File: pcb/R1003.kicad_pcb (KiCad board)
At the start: 2 copper layers, 45 x 33.3 mm, 27 parts, among them J1 PCIEXPRESS-X1, J2 CONN_01X03, J3 CONN254P-02X04, U1 EFM8BB10F2G

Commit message: getting ready for release
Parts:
- removed C1: 0.1u, Capacitors_SMD:C_0603
- removed G***: LOGO, pluggee:pluggee-LOGO-131X127
- removed G***: LOGO, pluggee:pluggee-QRNEG-127X127
- removed R1, R2, R3, R4, R5, R6, R7, R8: 10k, Resistors_SMD:R_0603
- removed U1: EFM8BB10F2G, Main:QFN50P300X300X75-20NT170X170
- added A1: ART, pluggee:pluggeeLabsIcon-11x6, F.Cu at (131.4, 75.3)
- added J10: SOCKET254P-01X02, Main:SOCKET254P-01X02_2, B.Cu at (143.0, 76.0)
- added J11: SOCKET254P-01X02, Main:SOCKET254P-01X02_2, B.Cu at (155.0, 76.0)
- added J12: SOCKET254P-01X02, Main:SOCKET254P-01X02_2, B.Cu at (155.0, 86.0)
- added J13: SOCKET254P-01X02, Main:SOCKET254P-01X02_2, B.Cu at (164.0, 90.0)
- added J4: SOCKET254P-01X02, Main:SOCKET254P-01X02_2, B.Cu at (164.0, 74.0)
- added J5: SOCKET254P-01X02, Main:SOCKET254P-01X02_2, B.Cu at (150.0, 86.0)
- added J6: SOCKET254P-01X02, Main:SOCKET254P-01X02_2, B.Cu at (138.0, 85.9)
- added J7: SOCKET254P-01X02, Main:SOCKET254P-01X02_2, B.Cu at (138.0, 76.0)
- added J8: SOCKET254P-01X02, Main:SOCKET254P-01X02_2, B.Cu at (150.0, 76.0)
- added J9: SOCKET254P-01X02, Main:SOCKET254P-01X02_2, B.Cu at (143.0, 85.9)
- C2, C3, C4, C5: value 0.1u -> CC0603KRX7R9BB104; footprint Capacitors_SMD:C_0603 -> Main:CAPC0603; moved to B.Cu
- J2, J3: moved to B.Cu
- R10, R11, R12, R9: value 5.6k -> RC0603FR-0710KL; footprint Resistors_SMD:R_0603 -> Main:RESC0603; moved to B.Cu
- R13, R14, R15, R16: value 4.7k -> RC0603FR-074K7L; footprint Resistors_SMD:R_0603 -> Main:RESC0603; moved to B.Cu
- moved J2 27.1 mm to (131.2, 85.9), turned to 270 degrees
- moved C4 19.0 mm to (135.0, 74.7), turned to 90 degrees
- moved C3 18.8 mm to (135.0, 87.3), turned to 270 degrees
- moved R11 13.3 mm to (146.0, 77.5), turned to 90 degrees
- moved R10 13.1 mm to (146.0, 84.5), turned to 270 degrees
- moved R16 12.7 mm to (160.0, 75.0), turned to 270 degrees
- moved C5 12.5 mm to (147.0, 74.6), turned to 90 degrees
- moved C2 12.0 mm to (147.2, 87.3), turned to 270 degrees
- moved R12 11.0 mm to (158.1, 75.0), turned to 90 degrees
- moved R9 10.6 mm to (158.1, 87.0), turned to 270 degrees
- moved R13 9.18 mm to (160.0, 87.0), turned to 90 degrees
- moved R15 5.69 mm to (160.0, 79.0), turned to 270 degrees
- moved R14 2.55 mm to (160.0, 83.0), turned to 90 degrees
- turned J3 to 90 degrees
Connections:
- C2 pad 1: PX4 -> /CX4
- C3 pad 1: PX3 -> /CX3
- C4 pad 1: PX2 -> /CX2
- C5 pad 1: PX1 -> /CX1
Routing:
- net +3V3: track 33.0 -> 96.4 mm, vias 4 -> 0
- net GND: track 61.5 -> 18.4 mm, vias 5 -> 0
- net P_JUMP: track 20.5 -> 57.0 mm, vias 0 -> 5
- net ID2: track 38.0 -> 2.30 mm, vias 1 -> 0
- net ID3: track 37.4 -> 2.30 mm, vias 1 -> 0
- net ID1: track 34.8 -> 2.30 mm, vias 1 -> 0
- net ID0: track 34.4 -> 2.30 mm, vias 1 -> 0
- net HT: track 51.8 -> 23.3 mm, vias 1 -> 0
- net ~MRESET: track 25.7 -> 2.30 mm
- net C2D: track 22.9 -> 2.30 mm, vias 1 -> 0
- net +5V: track 42.4 -> 62.0 mm, vias 1 -> 2
- net SCL: track 21.5 -> 2.30 mm
- net SDA: track 20.7 -> 2.30 mm
- net /X2: track 5.57 -> 22.0 mm
- net /X3: track 5.57 -> 21.5 mm
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- added copper zone on F.Cu, net GND
- removed copper zone on F.Cu, net +3V3
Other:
- board text added: "+3.3V"
- board text added: "+5V"
- board text added: "1 -"
- board text added: "2 -"
- board text added: "3 -"
- board text added: "4 -"
- board text added: "A1"
- board text added: "A2"
- board text added: "A3"
- board text added: "A4"
- board text added: "D1"
- board text added: "D2"
- board text added: "D3"
- board text added: "D4"
- board text added: "Pull-Up To:"
- board text added: "R1003 v1.0.1 Analog/Digital I/Os"
- board text added: "plugg.ee Labs LLC http://plugg.ee"
- board text removed: "R1003 v1.0.0 Analog/Digital I/Os plugg.ee Labs 2016 http://plugg.ee"

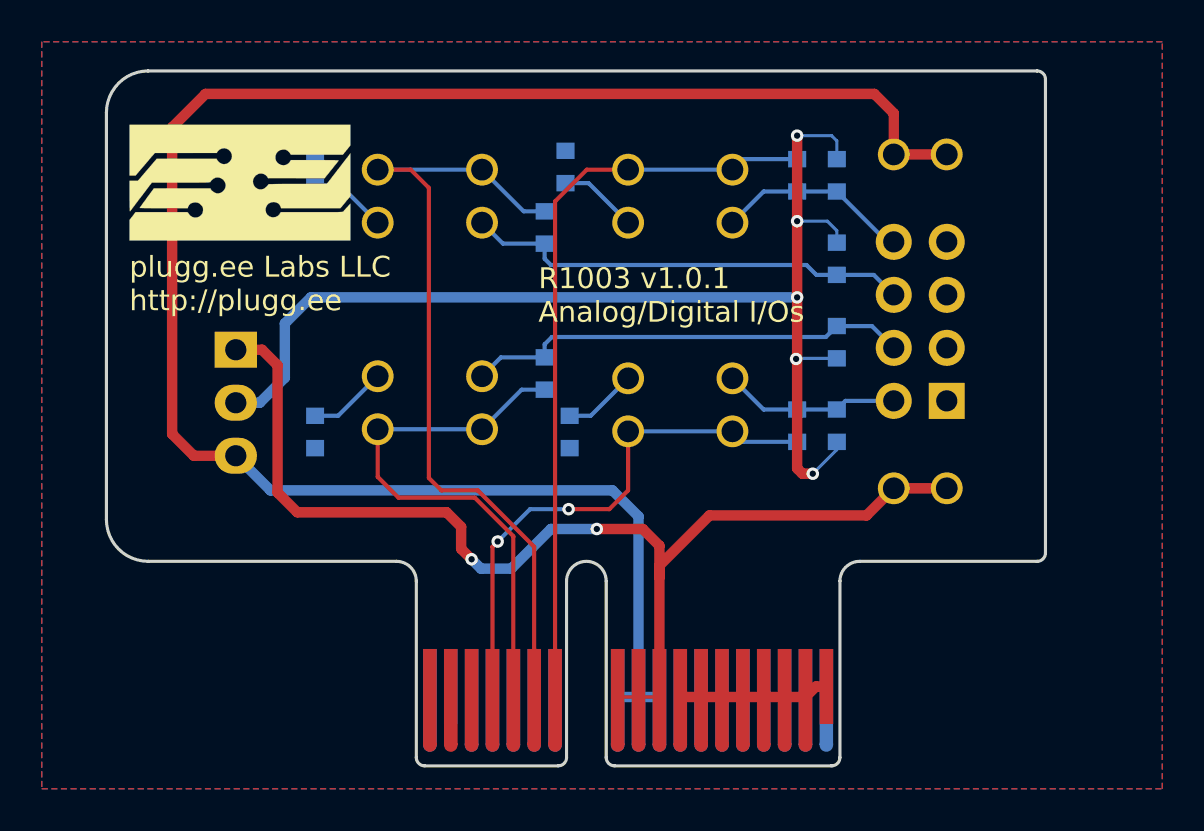
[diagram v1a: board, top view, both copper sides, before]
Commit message: added fiducials
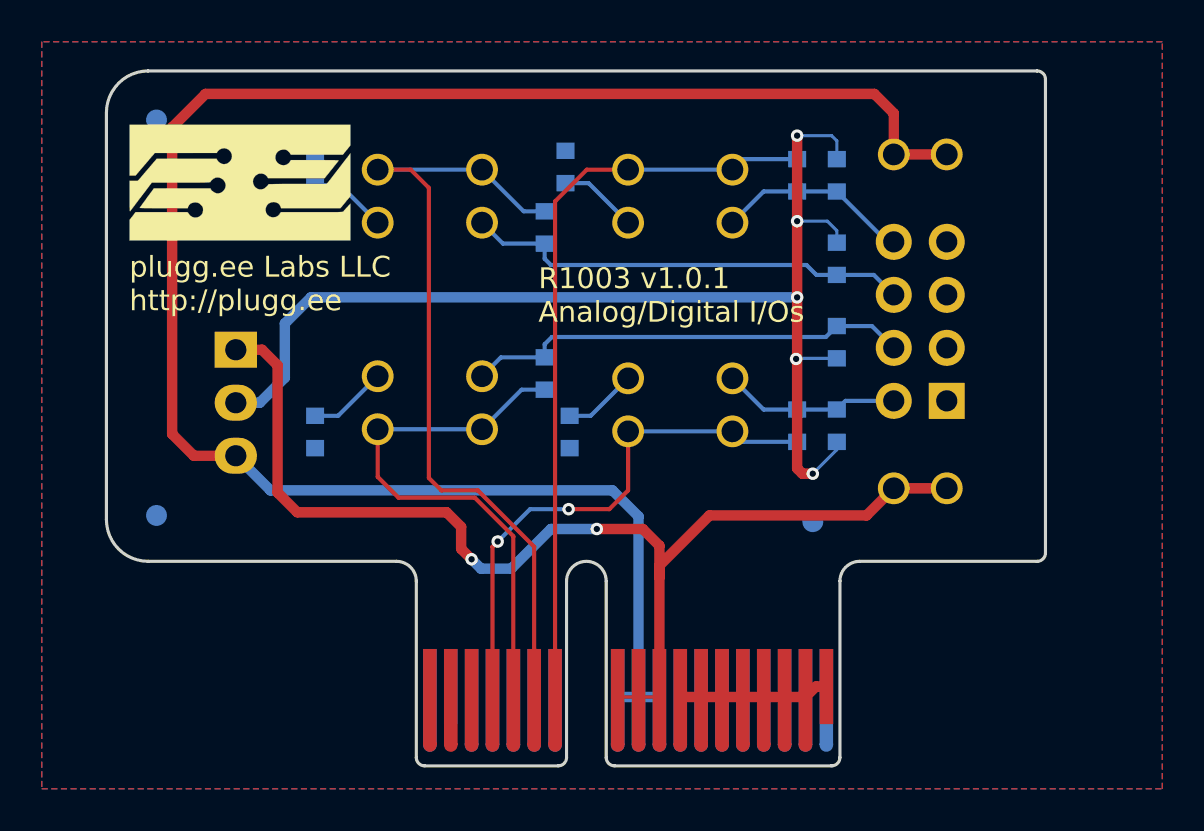
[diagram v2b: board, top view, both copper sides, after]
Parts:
- added FID1: FIDTOP001, Main:FIDTOP001, B.Cu at (127.4, 91.3)
- added FID2: FIDTOP001, Main:FIDTOP001, B.Cu at (158.8, 91.6)
- added FID3: FIDTOP001, Main:FIDTOP001, B.Cu at (127.4, 72.3)
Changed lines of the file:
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@@
   (general
     (links 98)
-    (no_connects 0)
+    (no_connects 15)
     (area 124.924999 69.924999 170.075001 103.375001)
     (thickness 1.6)
@@
     (tracks 182)
     (zones 0)
-    (modules 26)
+    (modules 29)
     (nets 27)
   )
@@
       (xy -5.002143 -0.338667) (xy -5.291666 -0.338667) (xy -5.291666 -2.772833) (xy 5.291667 -2.772833)
       (xy 5.291667 -1.781631)) (layer F.SilkS) (width 0.01))
+  )
+  (module Main:FIDTOP001 (layer B.Cu)
+    (at 127.4 91.3)
+    (descr "Circular Fiducial, 1mm bare copper top; 2.54mm keepout")
+    (tags marker)
+    (attr virtual)
+    (fp_text reference FID1 (at 0 -2.3) (layer B.SilkS) hide
+      (effects (font (size 0.7 0.7) (thickness 0.15)) (justify mirror))
+    )
+    (fp_text value FIDTOP001 (at 0 1.8) (layer B.Fab) hide
+      (effects (font (size 0.127 0.127) (thickness 0.03)) (justify mirror))
+    )
+    (fp_circle (center 0 0) (end 1.55 0) (layer B.CrtYd) (width 0.05))
+    (pad ~ smd circle (at 0 0) (size 1 1) (layers B.Cu B.Mask)
+      (solder_mask_margin 0.77) (clearance 0.77))
+  )
+  (module Main:FIDTOP001 (layer B.Cu)
+    (at 158.85 91.6)
+    (descr "Circular Fiducial, 1mm bare copper top; 2.54mm keepout")
+    (tags marker)
+    (attr virtual)
+    (fp_text reference FID2 (at 0 -2.3) (layer B.SilkS) hide
+      (effects (font (size 0.7 0.7) (thickness 0.15)) (justify mirror))
+    )
+    (fp_text value FIDTOP001 (at 0 1.8) (layer B.Fab) hide
+      (effects (font (size 0.127 0.127) (thickness 0.03)) (justify mirror))
+    )
+    (fp_circle (center 0 0) (end 1.55 0) (layer B.CrtYd) (width 0.05))
+    (pad ~ smd circle (at 0 0) (size 1 1) (layers B.Cu B.Mask)
+      (solder_mask_margin 0.77) (clearance 0.77))
+  )
+  (module Main:FIDTOP001 (layer B.Cu)
+    (at 127.4 72.35)
+    (descr "Circular Fiducial, 1mm bare copper top; 2.54mm keepout")
+    (tags marker)
+    (attr virtual)
+    (fp_text reference FID3 (at 0 -2.3) (layer B.SilkS) hide
+      (effects (font (size 0.7 0.7) (thickness 0.15)) (justify mirror))
+    )
+    (fp_text value FIDTOP001 (at 0 1.8) (layer B.Fab) hide
+      (effects (font (size 0.127 0.127) (thickness 0.03)) (justify mirror))
+    )
+    (fp_circle (center 0 0) (end 1.55 0) (layer B.CrtYd) (width 0.05))
+    (pad ~ smd circle (at 0 0) (size 1 1) (layers B.Cu B.Mask)
+      (solder_mask_margin 0.77) (clearance 0.77))
   )
   (gr_text "plugg.ee Labs LLC\nhttp://plugg.ee" (at 126.1 80.2) (layer F.SilkS)
@@
     (connect_pads (clearance 0.508))
     (min_thickness 0.254)
-    (fill yes (arc_segments 16) (thermal_gap 0.508) (thermal_bridge_width 0.508))
+    (fill (arc_segments 16) (thermal_gap 0.508) (thermal_bridge_width 0.508))
     (polygon
       (pts
@@
     (connect_pads (clearance 0.508))
     (min_thickness 0.254)
-    (fill yes (arc_segments 16) (thermal_gap 0.508) (thermal_bridge_width 0.508))
+    (fill (arc_segments 16) (thermal_gap 0.508) (thermal_bridge_width 0.508))
     (polygon
       (pts
@@
     (connect_pads (clearance 0.22))
     (min_thickness 0.2)
-    (fill yes (arc_segments 16) (thermal_gap 0) (thermal_bridge_width 0.25))
+    (fill (arc_segments 16) (thermal_gap 0) (thermal_bridge_width 0.25))
     (polygon
       (pts
@@
     (connect_pads (clearance 0.22))
     (min_thickness 0.2)
-    (fill yes (arc_segments 16) (thermal_gap 0) (thermal_bridge_width 0.25))
+    (fill (arc_segments 16) (thermal_gap 0) (thermal_bridge_width 0.25))
     (polygon
       (pts

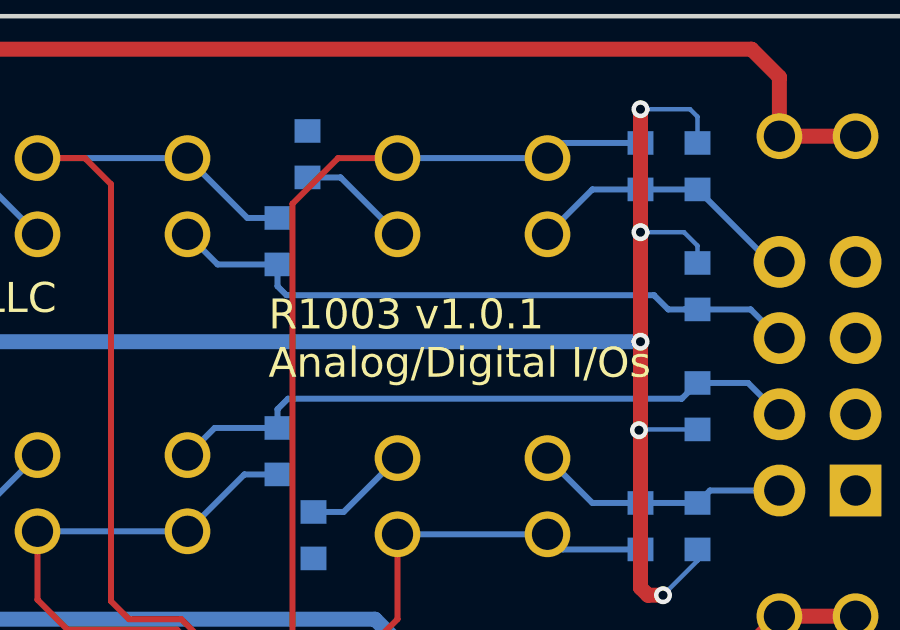
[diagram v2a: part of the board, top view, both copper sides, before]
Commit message: fixed silk screen version
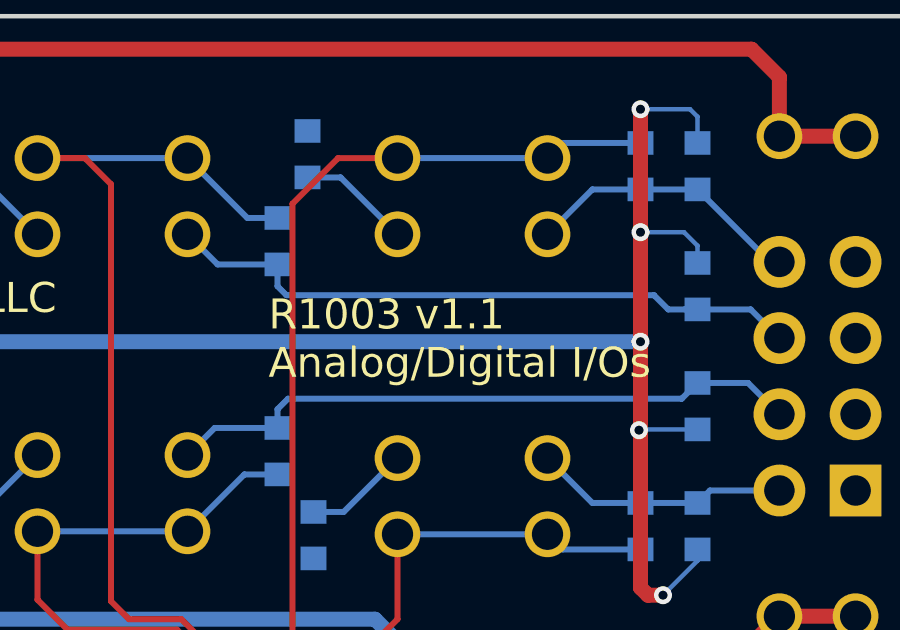
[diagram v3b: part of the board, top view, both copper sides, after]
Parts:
- J2: footprint Main:SOCKET254P-01X03 -> Main:CONN254P-01X03
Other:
- board text added: "R1003 v1.1 Analog/Digital I/Os"
- board text removed: "R1003 v1.0.1 Analog/Digital I/Os"
